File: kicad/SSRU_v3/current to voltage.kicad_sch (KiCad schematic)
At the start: 22 parts, among them J4 Conn_01x02, J5 Conn_01x02, J8 Conn_01x02, J9 Conn_01x02, U6 LM324

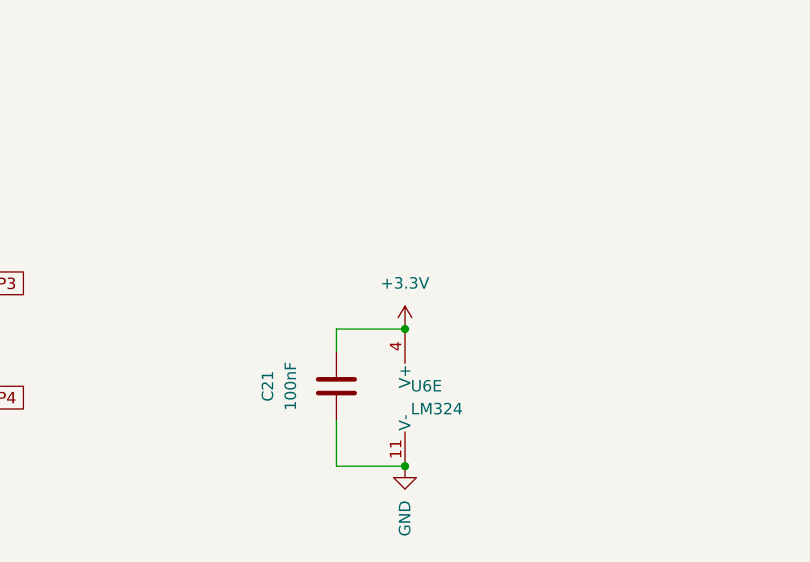
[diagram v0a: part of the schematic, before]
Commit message: ssru v3
current to voltage lm324 supply to  5v. icsp header mosi miso fixed
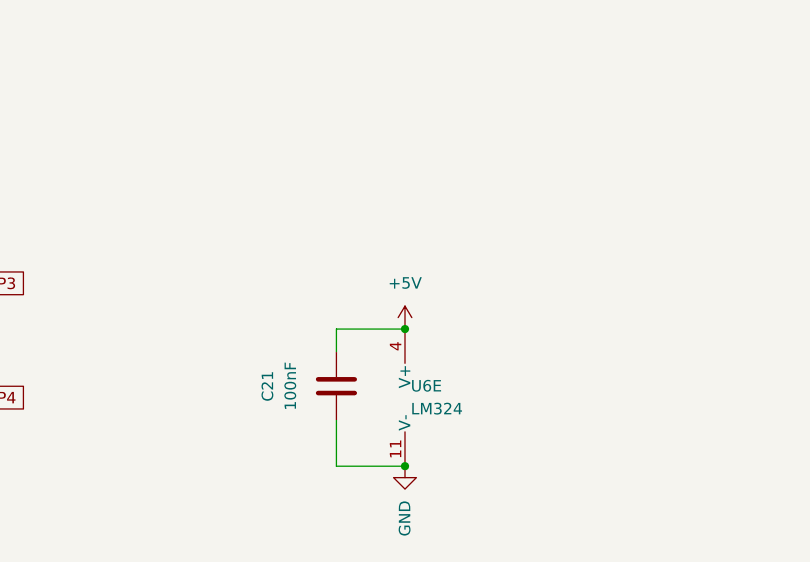
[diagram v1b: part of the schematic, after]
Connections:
- net +3.3V renamed +5V
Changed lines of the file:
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@@
+	)
+	(junction
+		(at 83.82 38.1)
+		(diameter 0)
+		(color 0 0 0 0)
+	)
+	(junction
+		(at 195.58 39.37)
+		(diameter 0)
+		(color 0 0 0 0)
+	)
+	(junction
+		(at 160.02 92.71)
+		(diameter 0)
+		(color 0 0 0 0)
+	)
+	(junction
+		(at 83.82 46.355)
+		(diameter 0)
+		(color 0 0 0 0)
+	)
+	(junction
+		(at 184.15 48.26)
+		(diameter 0)
+		(color 0 0 0 0)
+	)
+	(junction
+		(at 187.96 111.76)
+		(diameter 0)
+		(color 0 0 0 0)
+	)
+	(junction
+		(at 85.09 100.33)
+		(diameter 0)
+		(color 0 0 0 0)
+	)
+	(junction
+		(at 85.09 92.71)
+		(diameter 0)
+		(color 0 0 0 0)
+	)
+	(junction
+		(at 85.09 109.22)
+		(diameter 0)
+		(color 0 0 0 0)
+	)
+	(junction
+		(at 41.91 35.56)
+		(diameter 0)
+		(color 0 0 0 0)
 	)
 	(junction
 		(at 140.97 154.94)
-		(diameter 0)
-		(color 0 0 0 0)
-	)
-	(junction
-		(at 83.82 38.1)
-		(diameter 0)
-		(color 0 0 0 0)
-	)
-	(junction
-		(at 195.58 39.37)
-		(diameter 0)
-		(color 0 0 0 0)
-	)
-	(junction
-		(at 160.02 92.71)
-		(diameter 0)
-		(color 0 0 0 0)
-	)
-	(junction
-		(at 83.82 46.355)
-		(diameter 0)
-		(color 0 0 0 0)
-	)
-	(junction
-		(at 184.15 48.26)
-		(diameter 0)
-		(color 0 0 0 0)
-	)
-	(junction
-		(at 187.96 111.76)
-		(diameter 0)
-		(color 0 0 0 0)
-	)
-	(junction
-		(at 85.09 100.33)
-		(diameter 0)
-		(color 0 0 0 0)
-	)
-	(junction
-		(at 85.09 92.71)
-		(diameter 0)
-		(color 0 0 0 0)
-	)
-	(junction
-		(at 85.09 109.22)
-		(diameter 0)
-		(color 0 0 0 0)
-	)
-	(junction
-		(at 41.91 35.56)
 		(diameter 0)
 		(color 0 0 0 0)
@@
 	)
 	(symbol
-		(lib_id "power:+3.3V")
-		(at 140.97 154.94 0)
-		(unit 1)
-		(exclude_from_sim no)
-		(in_bom yes)
-		(on_board yes)
-		(dnp no)
-		(fields_autoplaced yes)
-		(property "Reference" "#PWR066"
-			(at 140.97 158.75 0)
-			(effects
-				(font
-					(size 1.27 1.27)
-				)
-				(hide yes)
-			)
-		)
-		(property "Value" "+3.3V"
-			(at 140.97 149.86 0)
-			(effects
-				(font
-					(size 1.27 1.27)
-				)
-			)
-		)
-		(property "Footprint" ""
-			(at 140.97 154.94 0)
-			(effects
-				(font
-					(size 1.27 1.27)
-				)
-				(hide yes)
-			)
-		)
-		(property "Datasheet" ""
-			(at 140.97 154.94 0)
-			(effects
-				(font
-					(size 1.27 1.27)
-				)
-				(hide yes)
-			)
-		)
-		(property "Description" "Power symbol creates a global label with name \"+3.3V\""
-			(at 140.97 154.94 0)
-			(effects
-				(font
-					(size 1.27 1.27)
-				)
-				(hide yes)
-			)
-		)
-		(pin "1"
-		)
-		(instances
-			(project "sensorboard_v10"
-				(path "/bee3e03c-9a5f-4c66-913e-823f7b125a2a/02657d5f-35c3-459a-91ca-e89a2aa05d13"
-					(reference "#PWR066")
-					(unit 1)
-				)
-			)
-		)
-	)
-	(symbol
 		(lib_id "Amplifier_Operational:LM324")
 		(at 170.815 39.37 0)
@@
 					(unit 1)
 				)
+			)
+		)
+	)
+	(symbol
+		(lib_id "power:+5V")
+		(at 140.97 154.94 0)
+		(unit 1)
+		(exclude_from_sim no)
+		(in_bom yes)
+		(on_board yes)
+		(dnp no)
+		(fields_autoplaced yes)
+		(property "Reference" "#PWR030"
+			(at 140.97 158.75 0)
+			(effects
+				(font
+					(size 1.27 1.27)
+				)
+				(hide yes)
+			)
+		)
+		(property "Value" "+5V"
+			(at 140.97 149.86 0)
+			(effects
+				(font
+					(size 1.27 1.27)
+				)
+			)
+		)
+		(property "Footprint" ""
+			(at 140.97 154.94 0)
+			(effects
+				(font
+					(size 1.27 1.27)
+				)
+				(hide yes)
+			)
+		)
+		(property "Datasheet" ""
+			(at 140.97 154.94 0)
+			(effects
+				(font
+					(size 1.27 1.27)
+				)
+				(hide yes)
+			)
+		)
+		(property "Description" "Power symbol creates a global label with name \"+5V\""
+			(at 140.97 154.94 0)
+			(effects
+				(font
+					(size 1.27 1.27)
+				)
+				(hide yes)
+			)
+		)
+		(pin "1"
+		)
+		(instances
+			(project ""
+				(path "/bee3e03c-9a5f-4c66-913e-823f7b125a2a/02657d5f-35c3-459a-91ca-e89a2aa05d13"
+					(reference "#PWR030")
+					(unit 1)
+				)

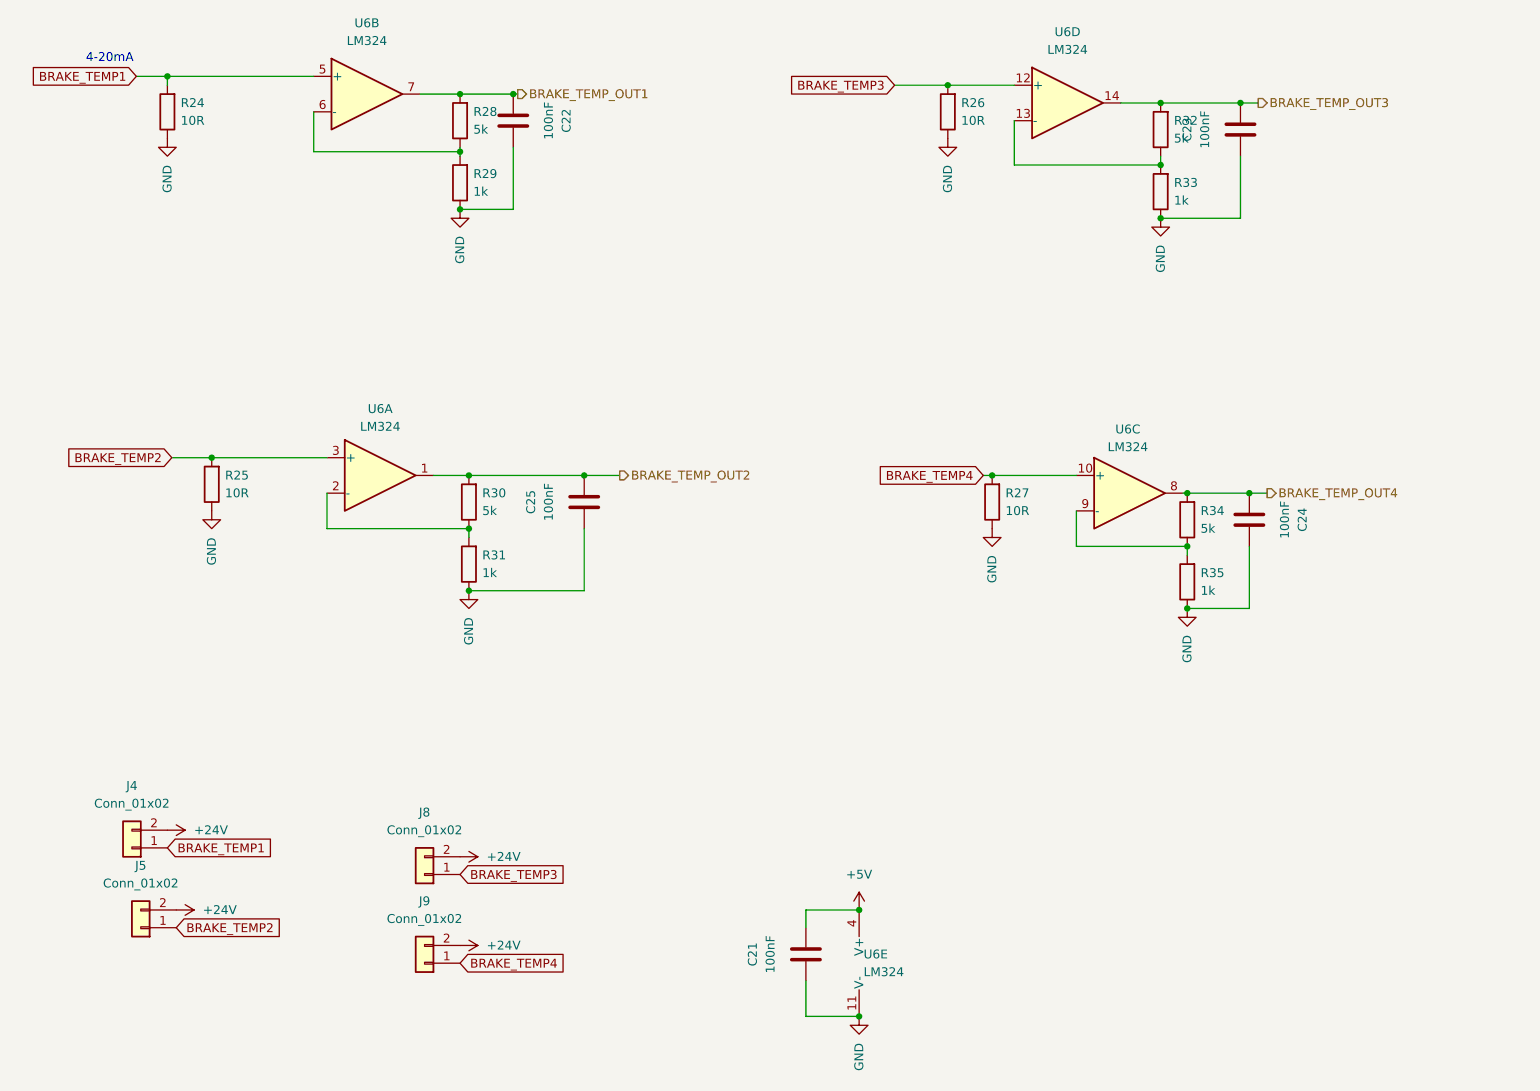
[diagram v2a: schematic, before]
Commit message: SSRU new scheme
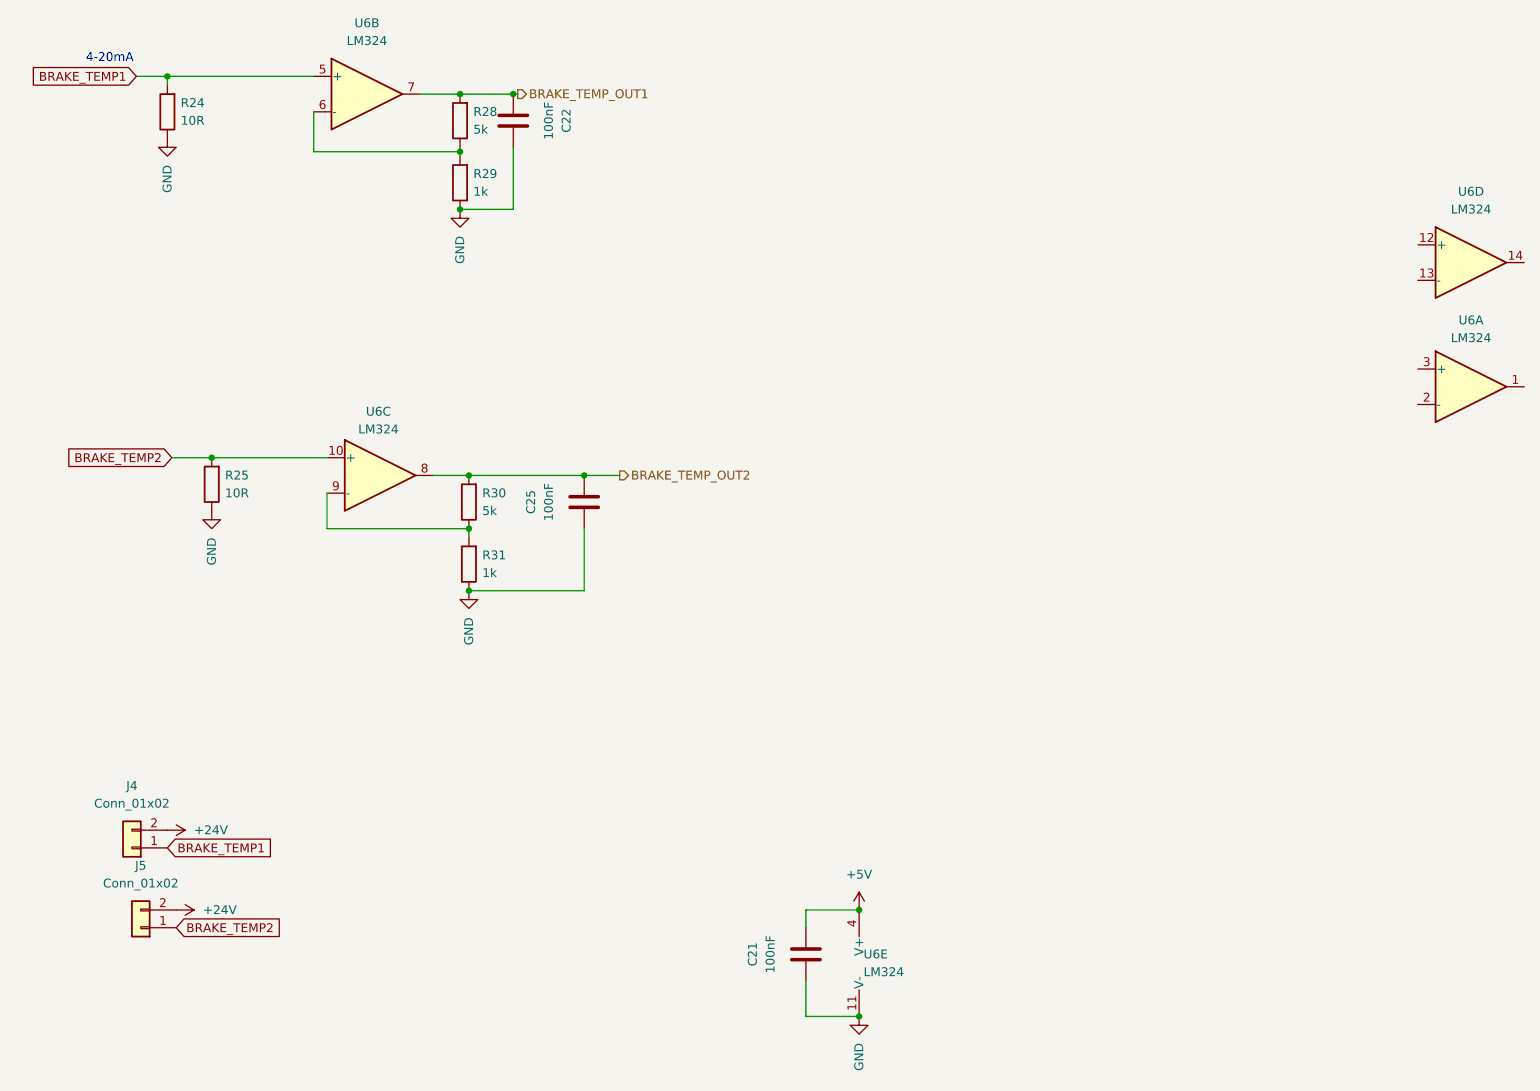
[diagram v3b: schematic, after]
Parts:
- removed C23, C24: 100nF, RMC_Capacitor:C_0805_2012Metric_Pad1.18x1.45mm_HandSolder_L, symbol Device:C
- removed J8, J9: Conn_01x02, Connector_JST:JST_XH_B2B-XH-A_1x02_P2.50mm_Vertical, symbol Connector_Generic:Conn_01x02
- removed R26, R27: 10R, RMC_Resistor:R_1206_3216Metric_Pad1.30x1.75mm_HandSolder_RMC, symbol Device:R
- removed R32, R34: 5k, RMC_Resistor:R_0805_2012Metric_Pad1.20x1.40mm_HandSolder_L, symbol Device:R
- removed R33, R35: 1k, RMC_Resistor:R_0805_2012Metric_Pad1.20x1.40mm_HandSolder_L, symbol Device:R
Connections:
- net BRAKE_TEMP4 is gone; now on net BRAKE_TEMP2: U6.10 (+)
- net BRAKE_TEMP_OUT4 is gone; now on net BRAKE_TEMP_OUT2: U6.8
- net BRAKE_TEMP2: no longer U6.3 (+)
- net BRAKE_TEMP_OUT2: no longer U6.1
- net at R30.1, R31.2: now also U6.9 (-); no longer U6.2 (-)
- net BRAKE_TEMP3: no longer names the net of U6.12 (+)
- net BRAKE_TEMP_OUT3: no longer names the net of U6.14
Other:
- moved on the sheet: U6C

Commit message: current to voltage
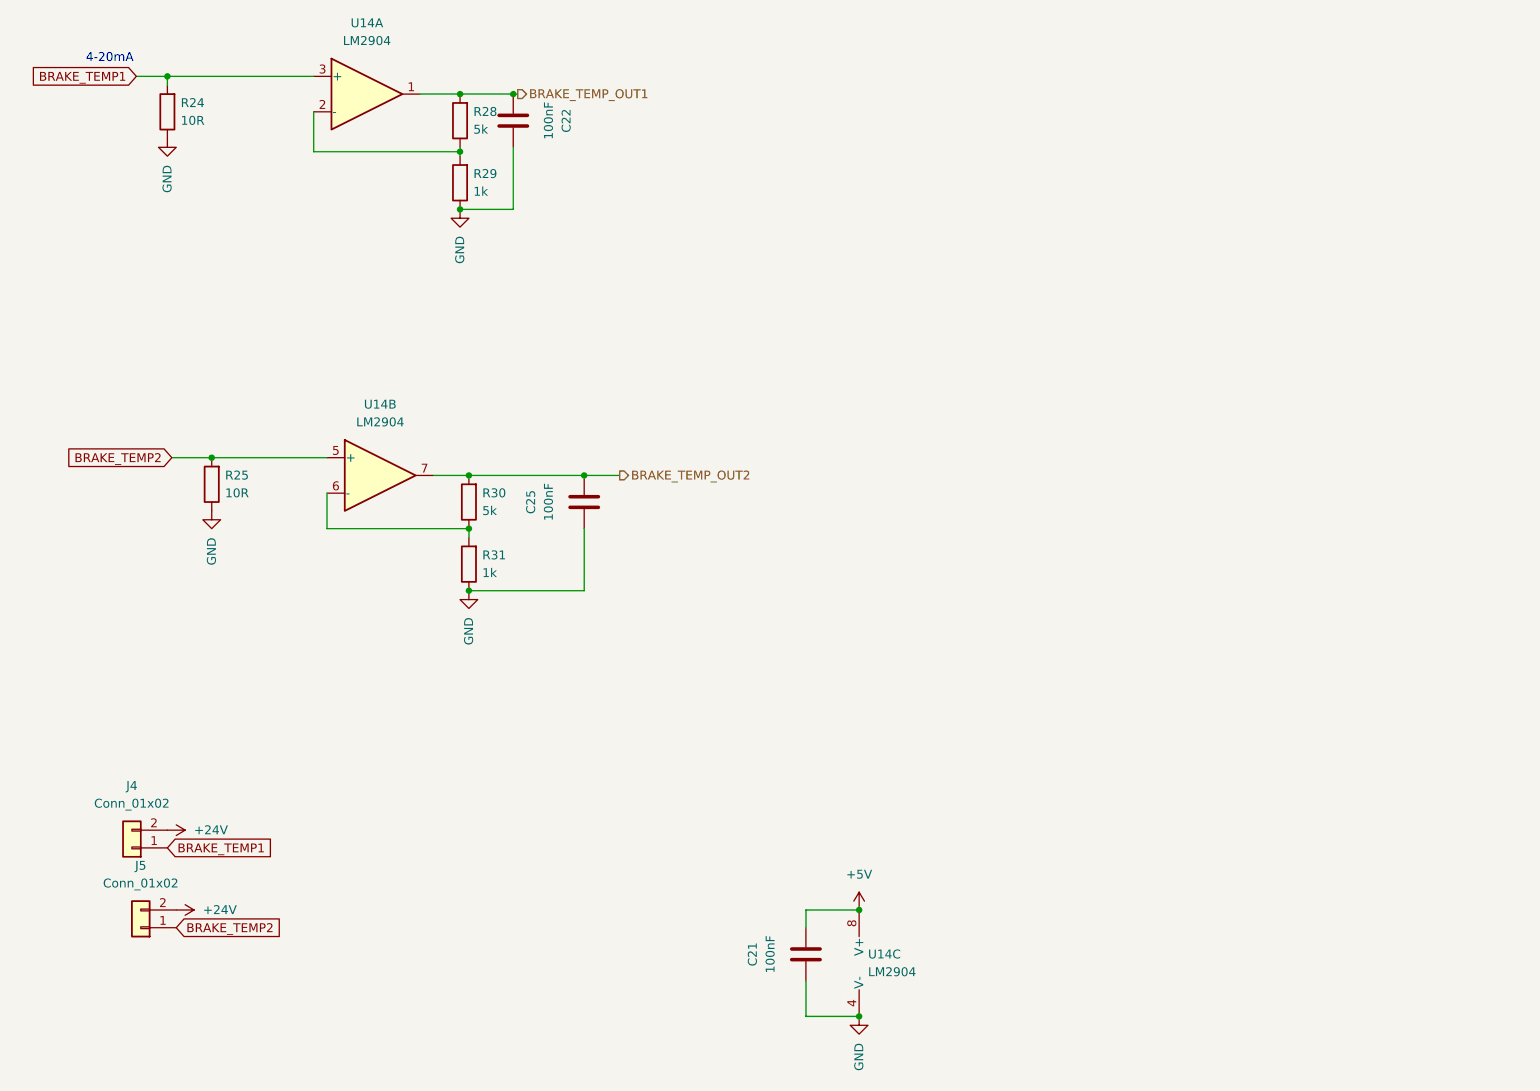
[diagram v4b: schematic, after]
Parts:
- removed U6: LM324, RMC_SO:SOIC127P600X175-14N, symbol Amplifier_Operational:LM324
- added U14: LM2904, RMC_SO:SOIC-8_3.9x4.9mm_P1.27mm_RMC_Handsolder, symbol Amplifier_Operational:LM2904
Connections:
- net +5V: now also U14.8 (V+)
- net BRAKE_TEMP1: now also U14.3 (+)
- net BRAKE_TEMP2: now also U14.5 (+)
- net BRAKE_TEMP_OUT1: now also U14.1
- net BRAKE_TEMP_OUT2: now also U14.7
- net GND: now also U14.4 (V-)
- net at R30.1, R31.2: now also U14.6 (-)
- net at R28.1, R29.2: now also U14.2 (-)

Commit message: SSRU V3
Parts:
- R28: value 5k -> 22k
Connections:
- net BRAKE_TEMP1: now also U14.5 (+); no longer U14.3 (+)
- net BRAKE_TEMP2: now also U14.3 (+); no longer U14.5 (+)
- net BRAKE_TEMP_OUT1: now also U14.7; no longer U14.1
- net BRAKE_TEMP_OUT2: now also U14.1; no longer U14.7
- net at R30.1, R31.2: now also U14.2 (-); no longer U14.6 (-)
- net at R28.1, R29.2: now also U14.6 (-); no longer U14.2 (-)
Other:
- moved on the sheet: R28, R29, U14A, U14B
